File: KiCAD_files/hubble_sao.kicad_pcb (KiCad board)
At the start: 2 copper layers, 38 x 45.5 mm, 43 parts, among them J1 Conn_02x03_Counter_Clockwise, J2 Conn_02x03_Odd_Even, Q1 DMP3099L-7, SW1 SW_Push_Shielded, SW2 SW_Push, U1 VEML3328, U2 LSM6DSO, U3 ATmega328PB-A, U4 TLV9062xD, U5 TLV9062xD

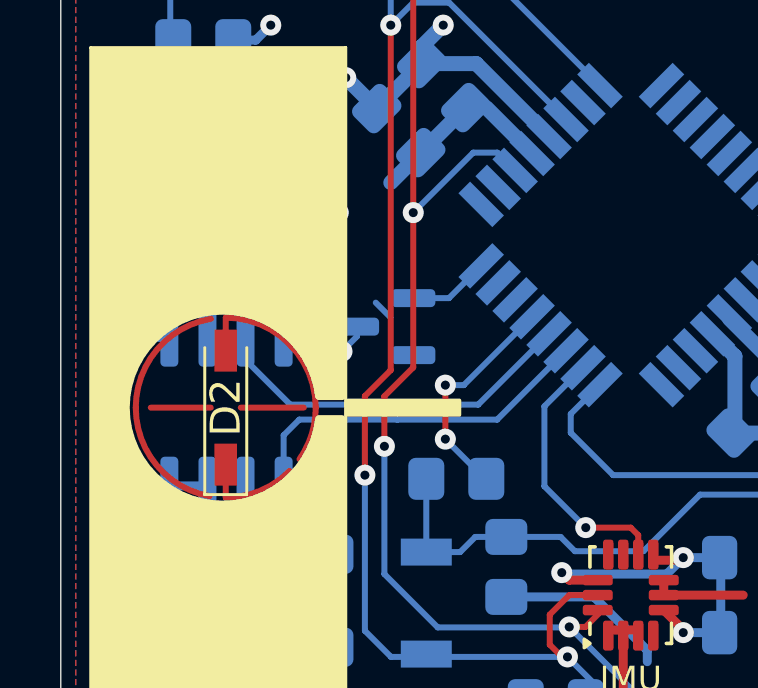
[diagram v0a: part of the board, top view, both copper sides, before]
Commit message: Reworked IR_TX LED
- Removed the copper pour keep out and round copper traces (they
were supposed too look nice, but in fact were not really visible)
- Simplified the routing of the power around the MOSFET
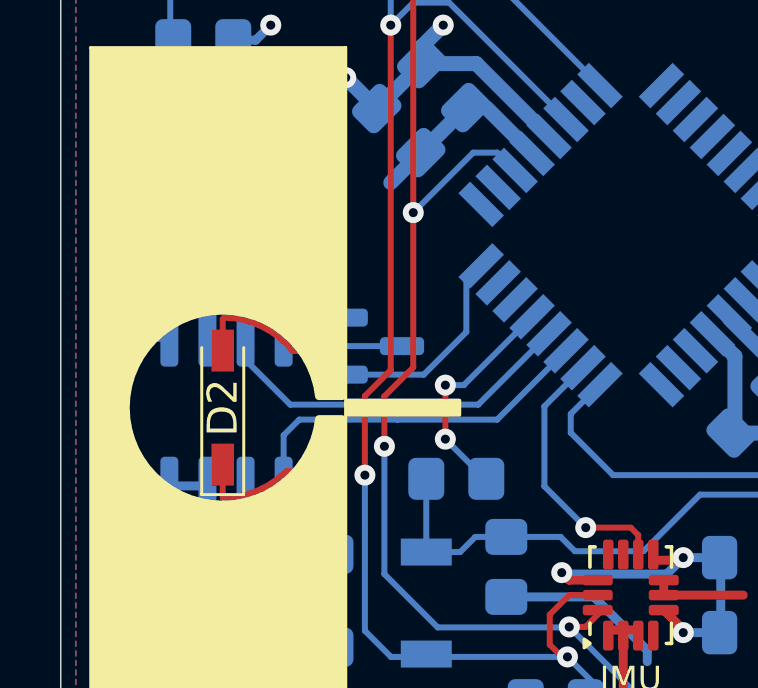
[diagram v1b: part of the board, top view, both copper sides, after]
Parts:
- moved Q1 0.75 mm to (81.4, 122.5), turned to 0 degrees
- moved C13 0.46 mm to (78.8, 118.5)
- moved D2 0.10 mm to (76.4, 124.5)
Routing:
- net /IR_TX: track 2.19 -> 6.77 mm
- net Net-(D2-A): track 4.33 -> 4.83 mm

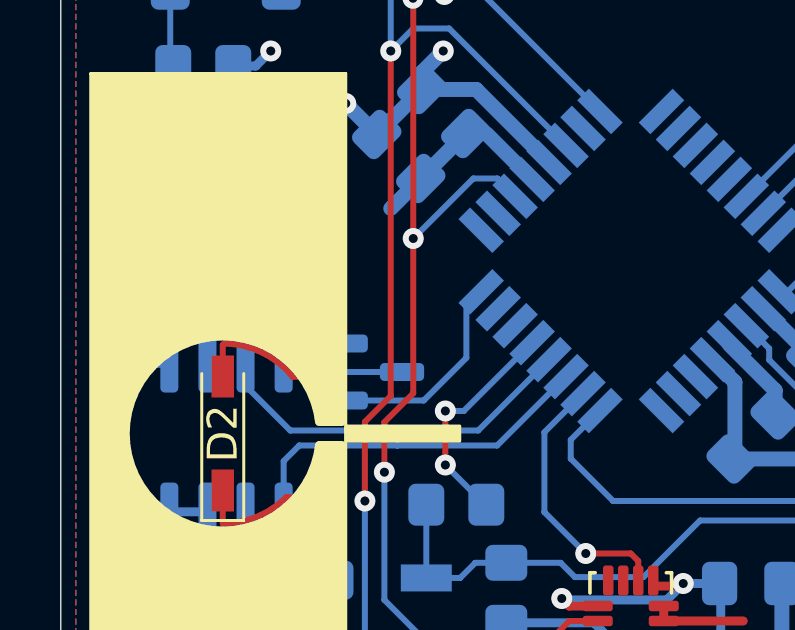
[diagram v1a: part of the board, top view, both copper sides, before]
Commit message: Added decoupling cap for the IR_TX LED (DNP for now) and touched up some tracks around there
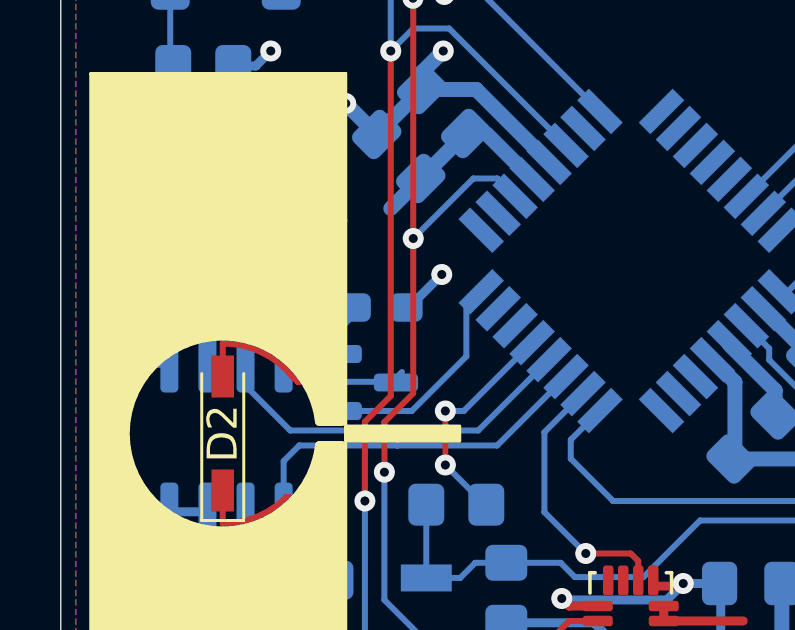
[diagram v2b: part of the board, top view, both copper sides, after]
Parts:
- added C15: C, Capacitor_SMD:C_0603_1608Metric_Pad1.08x0.95mm_HandSolder, B.Cu at (81.7, 120.3)
- moved Q1 0.40 mm to (81.2, 122.8)
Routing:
- net VCC: track 39.6 -> 43.0 mm
- net GND: track 65.0 -> 66.6 mm, vias 15 -> 16
